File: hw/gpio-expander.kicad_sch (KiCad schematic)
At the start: 8 parts, among them U2001 STM32C011F4U6TR, U2002 STM32C011F4U6TR, U2003 STM32C011F4U6TR, U2004 STM32C011F4U6TR

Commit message: Checkpoint before crazy script screws my files up (again)
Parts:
- renumbered C2001 to C1201, C2002 to C1202, C2003 to C1203, C2004 to C1204, U2001 to U1201, U2002 to U1202, U2003 to U1203, U2004 to U1204
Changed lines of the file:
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@@
 		(dnp no)
 		(fields_autoplaced yes)
-		(property "Reference" "U2001"
+		(property "Reference" "U1201"
 			(at 92.3133 39.37 0)
 			(effects
@@
 			(project "NexRx"
 				(path "/8ae46c04-d01a-4756-8774-512b694bfaff/0ee31834-a2c3-474b-9f7c-c9b4f3cadb3f/f2486bc2-eba8-4fb8-890d-ac8b4843b7f5"
-					(reference "U2001")
+					(reference "U1201")
 					(unit 1)
 				)
@@
 		(dnp no)
 		(fields_autoplaced yes)
-		(property "Reference" "#PWR02003"
+		(property "Reference" "#PWR01203"
 			(at 80.01 45.72 0)
 			(effects
@@
 			(project "NexRx"
 				(path "/8ae46c04-d01a-4756-8774-512b694bfaff/0ee31834-a2c3-474b-9f7c-c9b4f3cadb3f/f2486bc2-eba8-4fb8-890d-ac8b4843b7f5"
-					(reference "#PWR02003")
+					(reference "#PWR01203")
 					(unit 1)
 				)
@@
 		(dnp no)
 		(fields_autoplaced yes)
-		(property "Reference" "#PWR02013"
+		(property "Reference" "#PWR01213"
 			(at 144.78 45.72 0)
 			(effects
@@
 			(project "NexRx"
 				(path "/8ae46c04-d01a-4756-8774-512b694bfaff/0ee31834-a2c3-474b-9f7c-c9b4f3cadb3f/f2486bc2-eba8-4fb8-890d-ac8b4843b7f5"
-					(reference "#PWR02013")
+					(reference "#PWR01213")
 					(unit 1)
 				)
@@
 		(dnp no)
 		(fields_autoplaced yes)
-		(property "Reference" "U2003"
+		(property "Reference" "U1203"
 			(at 155.8133 115.57 0)
 			(effects
@@
 			(project "NexRx"
 				(path "/8ae46c04-d01a-4756-8774-512b694bfaff/0ee31834-a2c3-474b-9f7c-c9b4f3cadb3f/f2486bc2-eba8-4fb8-890d-ac8b4843b7f5"
-					(reference "U2003")
+					(reference "U1203")
 					(unit 1)
 				)
@@
 		(dnp no)
 		(fields_autoplaced yes)
-		(property "Reference" "#PWR02010"
+		(property "Reference" "#PWR01210"
 			(at 133.35 148.59 0)
 			(effects
@@
 			(project "NexRx"
 				(path "/8ae46c04-d01a-4756-8774-512b694bfaff/0ee31834-a2c3-474b-9f7c-c9b4f3cadb3f/f2486bc2-eba8-4fb8-890d-ac8b4843b7f5"
-					(reference "#PWR02010")
+					(reference "#PWR01210")
 					(unit 1)
 				)
@@
 		(dnp no)
 		(fields_autoplaced yes)
-		(property "Reference" "U2002"
+		(property "Reference" "U1202"
 			(at 93.5833 116.84 0)
 			(effects
@@
 			(project "NexRx"
 				(path "/8ae46c04-d01a-4756-8774-512b694bfaff/0ee31834-a2c3-474b-9f7c-c9b4f3cadb3f/f2486bc2-eba8-4fb8-890d-ac8b4843b7f5"
-					(reference "U2002")
+					(reference "U1202")
 					(unit 1)
 				)
@@
 		(dnp no)
 		(fields_autoplaced yes)
-		(property "Reference" "#PWR02009"
+		(property "Reference" "#PWR01209"
 			(at 130.81 63.5 0)
 			(effects
@@
 			(project "NexRx"
 				(path "/8ae46c04-d01a-4756-8774-512b694bfaff/0ee31834-a2c3-474b-9f7c-c9b4f3cadb3f/f2486bc2-eba8-4fb8-890d-ac8b4843b7f5"
-					(reference "#PWR02009")
+					(reference "#PWR01209")
 					(unit 1)
 				)
@@
 		(dnp no)
 		(fields_autoplaced yes)
-		(property "Reference" "U2004"
+		(property "Reference" "U1204"
 			(at 157.0833 39.37 0)
 			(effects
@@
 			(project "NexRx"
 				(path "/8ae46c04-d01a-4756-8774-512b694bfaff/0ee31834-a2c3-474b-9f7c-c9b4f3cadb3f/f2486bc2-eba8-4fb8-890d-ac8b4843b7f5"
-					(reference "U2004")
+					(reference "U1204")
 					(unit 1)
 				)
@@
 		(dnp no)
 		(fields_autoplaced yes)
-		(property "Reference" "#PWR02011"
+		(property "Reference" "#PWR01211"
 			(at 134.62 72.39 0)
 			(effects
@@
 			(project "NexRx"
 				(path "/8ae46c04-d01a-4756-8774-512b694bfaff/0ee31834-a2c3-474b-9f7c-c9b4f3cadb3f/f2486bc2-eba8-4fb8-890d-ac8b4843b7f5"
-					(reference "#PWR02011")
+					(reference "#PWR01211")
 					(unit 1)
 				)
@@
 		(dnp no)
 		(fields_autoplaced yes)
-		(property "Reference" "C2001"
+		(property "Reference" "C1201"
 			(at 82.6769 35.56 0)
 			(effects
@@
 			(project "NexRx"
 				(path "/8ae46c04-d01a-4756-8774-512b694bfaff/0ee31834-a2c3-474b-9f7c-c9b4f3cadb3f/f2486bc2-eba8-4fb8-890d-ac8b4843b7f5"
-					(reference "C2001")
+					(reference "C1201")
 					(unit 1)
 				)
@@
 		(dnp no)
 		(fields_autoplaced yes)
-		(property "Reference" "#PWR02007"
+		(property "Reference" "#PWR01207"
 			(at 91.44 118.11 0)
 			(effects
@@
 			(project "NexRx"
 				(path "/8ae46c04-d01a-4756-8774-512b694bfaff/0ee31834-a2c3-474b-9f7c-c9b4f3cadb3f/f2486bc2-eba8-4fb8-890d-ac8b4843b7f5"
-					(reference "#PWR02007")
+					(reference "#PWR01207")
 					(unit 1)
 				)
@@
 		(dnp no)
 		(fields_autoplaced yes)
-		(property "Reference" "#PWR02008"
+		(property "Reference" "#PWR01208"
 			(at 91.44 172.72 0)
 			(effects
@@
 			(project "NexRx"
 				(path "/8ae46c04-d01a-4756-8774-512b694bfaff/0ee31834-a2c3-474b-9f7c-c9b4f3cadb3f/f2486bc2-eba8-4fb8-890d-ac8b4843b7f5"
-					(reference "#PWR02008")
+					(reference "#PWR01208")
 					(unit 1)
 				)
@@
 		(dnp no)
 		(fields_autoplaced yes)
-		(property "Reference" "C2003"
+		(property "Reference" "C1203"
 			(at 146.1769 111.76 0)
 			(effects
@@
 			(project "NexRx"
 				(path "/8ae46c04-d01a-4756-8774-512b694bfaff/0ee31834-a2c3-474b-9f7c-c9b4f3cadb3f/f2486bc2-eba8-4fb8-890d-ac8b4843b7f5"
-					(reference "C2003")
+					(reference "C1203")
 					(unit 1)
 				)
@@
 		(dnp no)
 		(fields_autoplaced yes)
-		(property "Reference" "C2004"
+		(property "Reference" "C1204"
 			(at 147.4469 35.56 0)
 			(effects
@@
 			(project "NexRx"
 				(path "/8ae46c04-d01a-4756-8774-512b694bfaff/0ee31834-a2c3-474b-9f7c-c9b4f3cadb3f/f2486bc2-eba8-4fb8-890d-ac8b4843b7f5"
-					(reference "C2004")
+					(reference "C1204")
 					(unit 1)
 				)
@@
 		(dnp no)
 		(fields_autoplaced yes)
-		(property "Reference" "#PWR02012"
+		(property "Reference" "#PWR01212"
 			(at 143.51 121.92 0)
 			(effects
@@
 			(project "NexRx"
 				(path "/8ae46c04-d01a-4756-8774-512b694bfaff/0ee31834-a2c3-474b-9f7c-c9b4f3cadb3f/f2486bc2-eba8-4fb8-890d-ac8b4843b7f5"
-					(reference "#PWR02012")
+					(reference "#PWR01212")
 					(unit 1)
 				)
@@
 		(dnp no)
 		(fields_autoplaced yes)
-		(property "Reference" "#PWR02016"
+		(property "Reference" "#PWR01216"
 			(at 154.94 40.64 0)
 			(effects
@@
 			(project "NexRx"
 				(path "/8ae46c04-d01a-4756-8774-512b694bfaff/0ee31834-a2c3-474b-9f7c-c9b4f3cadb3f/f2486bc2-eba8-4fb8-890d-ac8b4843b7f5"
-					(reference "#PWR02016")
+					(reference "#PWR01216")
 					(unit 1)
 				)
@@
 		(dnp no)
 		(fields_autoplaced yes)
-		(property "Reference" "#PWR02005"
+		(property "Reference" "#PWR01205"
 			(at 90.17 40.64 0)
 			(effects
@@
 			(project "NexRx"
 				(path "/8ae46c04-d01a-4756-8774-512b694bfaff/0ee31834-a2c3-474b-9f7c-c9b4f3cadb3f/f2486bc2-eba8-4fb8-890d-ac8b4843b7f5"
-					(reference "#PWR02005")
+					(reference "#PWR01205")
 					(unit 1)
 				)
@@
 		(dnp no)
 		(fields_autoplaced yes)
-		(property "Reference" "#PWR02015"
+		(property "Reference" "#PWR01215"
 			(at 153.67 171.45 0)
 			(effects
@@
 			(project "NexRx"
 				(path "/8ae46c04-d01a-4756-8774-512b694bfaff/0ee31834-a2c3-474b-9f7c-c9b4f3cadb3f/f2486bc2-eba8-4fb8-890d-ac8b4843b7f5"
-					(reference "#PWR02015")
+					(reference "#PWR01215")
 					(unit 1)
 				)
@@
 		(dnp no)
 		(fields_autoplaced yes)
-		(property "Reference" "C2002"
+		(property "Reference" "C1202"
 			(at 83.9469 113.03 0)
 			(effects
@@
 			(project "NexRx"
 				(path "/8ae46c04-d01a-4756-8774-512b694bfaff/0ee31834-a2c3-474b-9f7c-c9b4f3cadb3f/f2486bc2-eba8-4fb8-890d-ac8b4843b7f5"
-					(reference "C2002")
+					(reference "C1202")
 					(unit 1)
 				)
@@
 		(dnp no)
 		(fields_autoplaced yes)
-		(property "Reference" "#PWR02004"
+		(property "Reference" "#PWR01204"
 			(at 81.28 123.19 0)
 			(effects
@@
 			(project "NexRx"
 				(path "/8ae46c04-d01a-4756-8774-512b694bfaff/0ee31834-a2c3-474b-9f7c-c9b4f3cadb3f/f2486bc2-eba8-4fb8-890d-ac8b4843b7f5"
-					(reference "#PWR02004")
+					(reference "#PWR01204")
 					(unit 1)
 				)
@@
 		(dnp no)
 		(fields_autoplaced yes)
-		(property "Reference" "#PWR02017"
+		(property "Reference" "#PWR01217"
 			(at 154.94 95.25 0)
 			(effects
@@
 			(project "NexRx"
 				(path "/8ae46c04-d01a-4756-8774-512b694bfaff/0ee31834-a2c3-474b-9f7c-c9b4f3cadb3f/f2486bc2-eba8-4fb8-890d-ac8b4843b7f5"
-					(reference "#PWR02017")
+					(reference "#PWR01217")
 					(unit 1)
 				)
@@
 		(dnp no)
 		(fields_autoplaced yes)
-		(property "Reference" "#PWR02014"
+		(property "Reference" "#PWR01214"
 			(at 153.67 116.84 0)
 			(effects
@@
 			(project "NexRx"
 				(path "/8ae46c04-d01a-4756-8774-512b694bfaff/0ee31834-a2c3-474b-9f7c-c9b4f3cadb3f/f2486bc2-eba8-4fb8-890d-ac8b4843b7f5"
-					(reference "#PWR02014")
+					(reference "#PWR01214")
 					(unit 1)
 				)
@@
 		(dnp no)
 		(fields_autoplaced yes)
-		(property "Reference" "#PWR02006"
+		(property "Reference" "#PWR01206"
 			(at 90.17 95.25 0)
 			(effects
@@
 			(project "NexRx"
 				(path "/8ae46c04-d01a-4756-8774-512b694bfaff/0ee31834-a2c3-474b-9f7c-c9b4f3cadb3f/f2486bc2-eba8-4fb8-890d-ac8b4843b7f5"
-					(reference "#PWR02006")
+					(reference "#PWR01206")
 					(unit 1)
 				)
@@
 		(dnp no)
 		(fields_autoplaced yes)
-		(property "Reference" "#PWR02001"
+		(property "Reference" "#PWR01201"
 			(at 69.85 72.39 0)
 			(effects
@@
 			(project "NexRx"
 				(path "/8ae46c04-d01a-4756-8774-512b694bfaff/0ee31834-a2c3-474b-9f7c-c9b4f3cadb3f/f2486bc2-eba8-4fb8-890d-ac8b4843b7f5"
-					(reference "#PWR02001")
+					(reference "#PWR01201")
 					(unit 1)
 				)
@@
 		(dnp no)
 		(fields_autoplaced yes)
-		(property "Reference" "#PWR02002"
+		(property "Reference" "#PWR01202"
 			(at 71.12 149.86 0)
 			(effects
@@
 			(project "NexRx"
 				(path "/8ae46c04-d01a-4756-8774-512b694bfaff/0ee31834-a2c3-474b-9f7c-c9b4f3cadb3f/f2486bc2-eba8-4fb8-890d-ac8b4843b7f5"
-					(reference "#PWR02002")
-					(unit 1)
-				)
+					(reference "#PWR01202")
+					(unit 1)
+				)

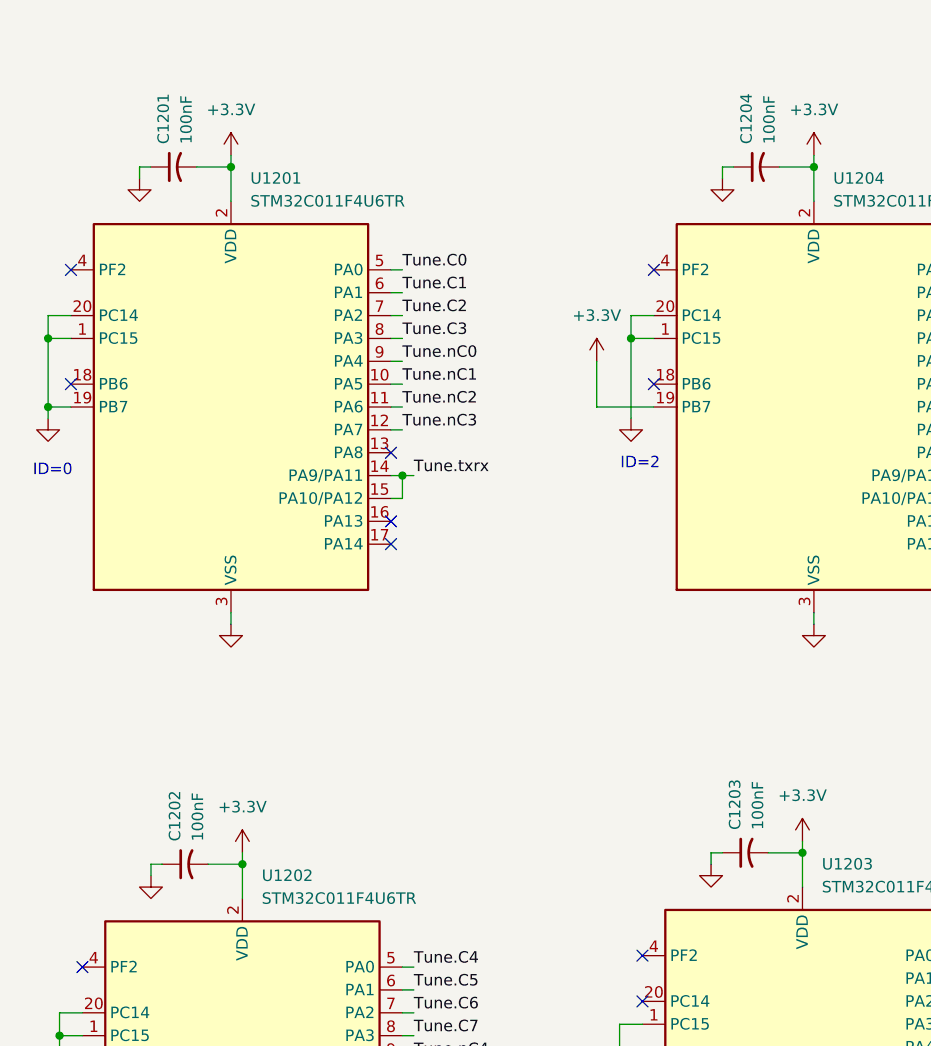
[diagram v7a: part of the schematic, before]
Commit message: Ready to buy the first BOM parts for DVT1 PCBs that have small solder bridge issues for USB-C connector
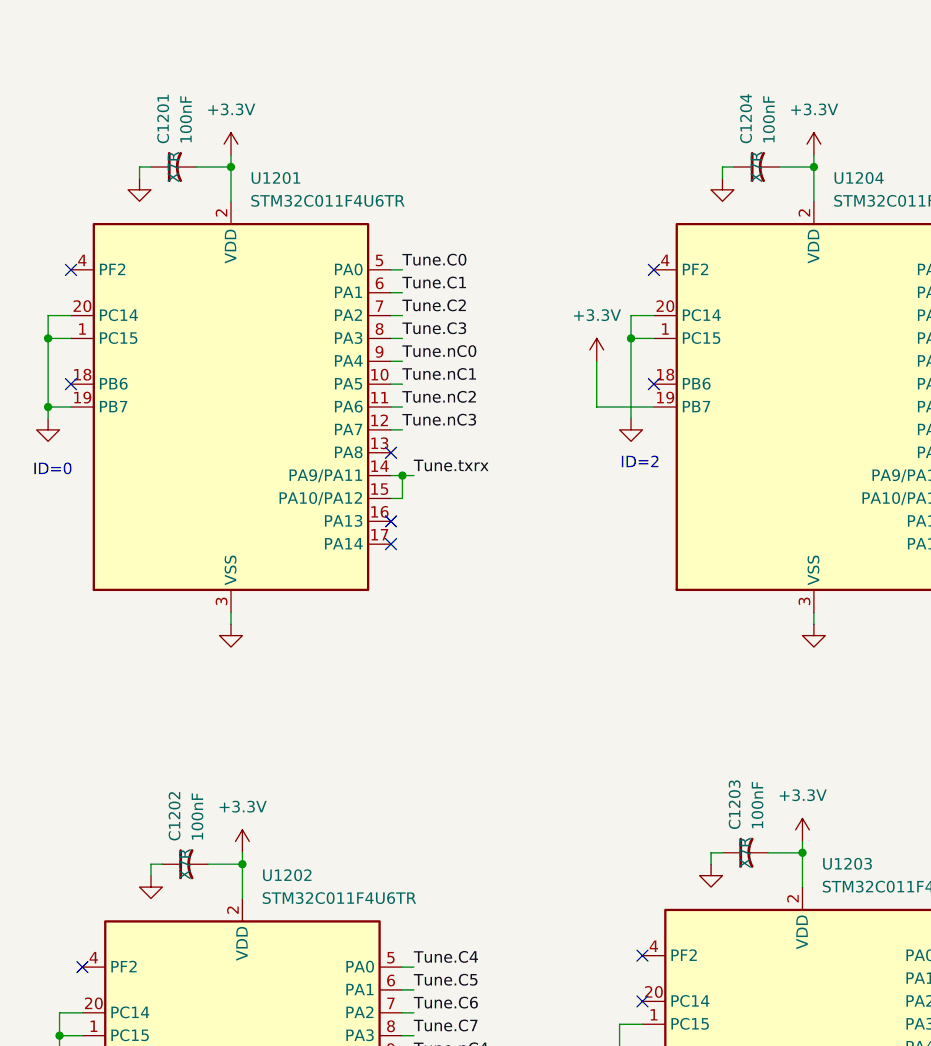
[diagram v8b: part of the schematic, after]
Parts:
- C1201, C1202, C1203, C1204: footprint Capacitor_SMD:C_0402_1005Metric -> Capacitor_SMD:C_0603_1608Metric; cap-type (none) -> X7R; working-voltage (none) -> 50V
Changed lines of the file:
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@@
 			)
 		)
-		(property "Footprint" "Capacitor_SMD:C_0402_1005Metric"
+		(property "Footprint" "Capacitor_SMD:C_0603_1608Metric"
 			(at 83.82 38.1 0)
 			(effects
@@
 			)
 		)
-		(property "cap-type" ""
+		(property "cap-type" "X7R"
 			(at 83.82 38.1 0)
 			(effects
@@
 			)
 		)
+		(property "working-voltage" "50V"
+			(at 83.82 38.1 0)
+			(effects
+				(font
+					(size 1.27 1.27)
+				)
+				(hide yes)
+			)
+		)
 		(pin "2"
 		)
@@
 			)
 		)
-		(property "Footprint" "Capacitor_SMD:C_0402_1005Metric"
+		(property "Footprint" "Capacitor_SMD:C_0603_1608Metric"
 			(at 147.32 114.3 0)
 			(effects
@@
 			)
 		)
-		(property "cap-type" ""
+		(property "cap-type" "X7R"
 			(at 147.32 114.3 0)
 			(effects
@@
 			)
 		)
+		(property "working-voltage" "50V"
+			(at 147.32 114.3 0)
+			(effects
+				(font
+					(size 1.27 1.27)
+				)
+				(hide yes)
+			)
+		)
 		(pin "2"
 		)
@@
 			)
 		)
-		(property "Footprint" "Capacitor_SMD:C_0402_1005Metric"
+		(property "Footprint" "Capacitor_SMD:C_0603_1608Metric"
 			(at 148.59 38.1 0)
 			(effects
@@
 			)
 		)
-		(property "cap-type" ""
+		(property "cap-type" "X7R"
 			(at 148.59 38.1 0)
 			(effects
@@
 			)
 		)
+		(property "working-voltage" "50V"
+			(at 148.59 38.1 0)
+			(effects
+				(font
+					(size 1.27 1.27)
+				)
+				(hide yes)
+			)
+		)
 		(pin "2"
 		)
@@
 			)
 		)
-		(property "Footprint" "Capacitor_SMD:C_0402_1005Metric"
+		(property "Footprint" "Capacitor_SMD:C_0603_1608Metric"
 			(at 85.09 115.57 0)
 			(effects
@@
 			)
 		)
-		(property "cap-type" ""
+		(property "cap-type" "X7R"
 			(at 85.09 115.57 0)
 			(effects
@@
 			(at 85.09 115.57 0)
 			(effects
+				(font
+					(size 1.27 1.27)
+				)
+				(hide yes)
+			)
+		)
+		(property "working-voltage" "50V"
+			(at 85.09 115.57 0)
+			(effects
